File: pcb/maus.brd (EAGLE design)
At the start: 100 x 101 mm, 79 parts, among them IC1 AP1509-50SG-13, J1 SS-52300-001, Q2 BSS123, Q3 BSS123, Q4 BSS123, Q6 PMN30XPEA, Q7 PMN30XPEA, U2 CH340C, U4 LP3965EMP-3.3, U6 LM358DR, U69 ESP32-S2-WROOM

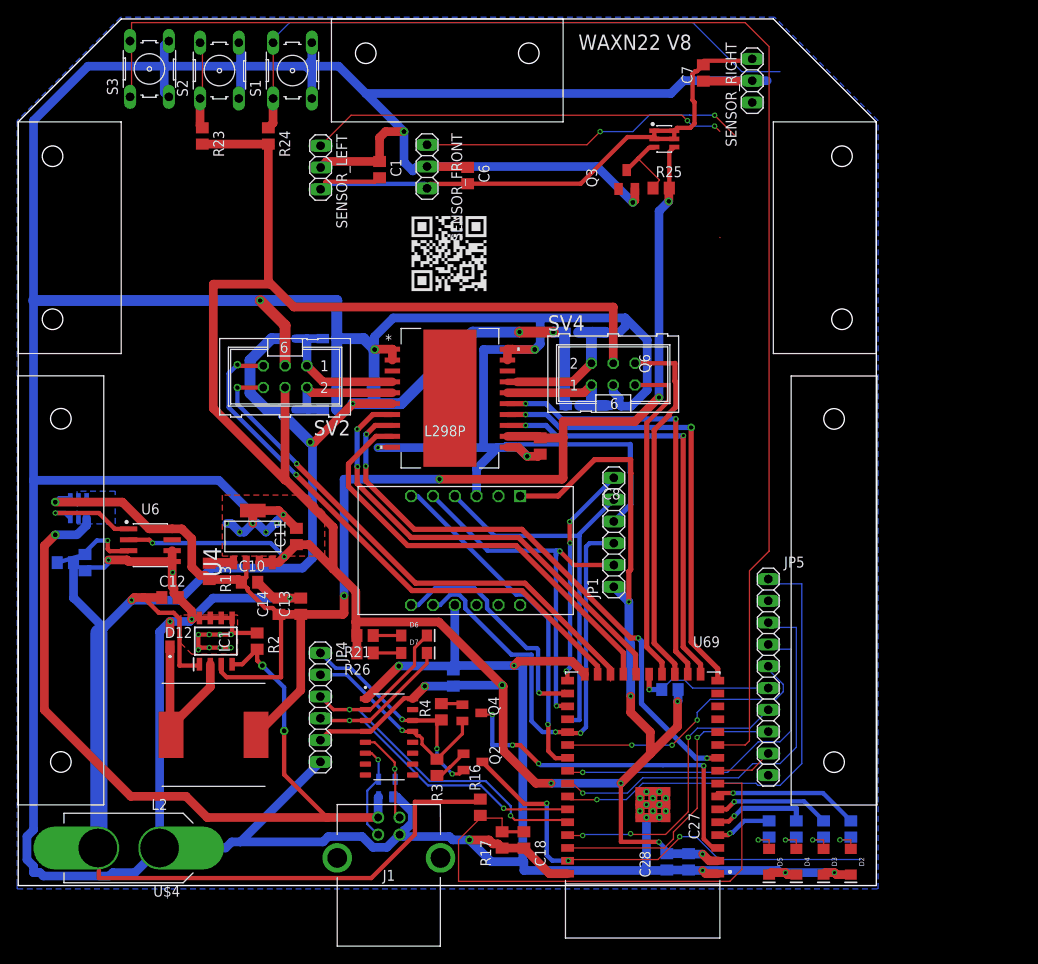
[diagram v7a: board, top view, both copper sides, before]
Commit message: update sensor + btn wiring
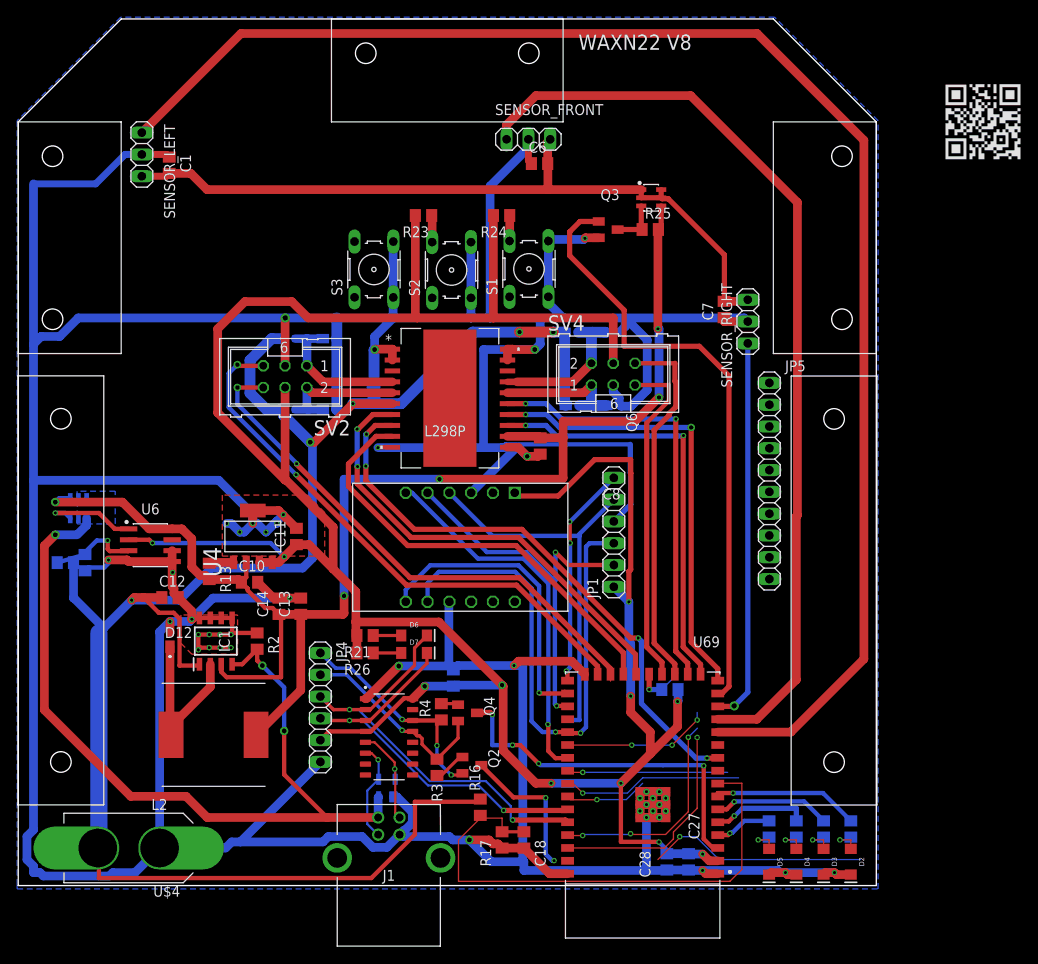
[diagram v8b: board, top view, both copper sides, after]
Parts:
- moved S1 36.0 mm to (75.5, 86.9)
- moved S2 35.7 mm to (66.5, 86.7)
- moved S3 35.1 mm to (57.5, 86.8)
- moved R24 28.7 mm to (72.3, 93.1), turned to 180 degrees
- moved SENSOR_RIGHT 28.1 mm to (101.0, 80.7)
- moved C7 27.7 mm to (98.3, 82.1)
- moved R23 27.4 mm to (63.2, 93.1), turned to 180 degrees
- moved C1 24.5 mm to (33.6, 98.9)
- moved JP5 22.9 mm to (103.5, 62.1)
- moved SENSOR_LEFT 20.9 mm to (30.4, 100.2)
- moved SENSOR_FRONT 12.2 mm to (75.5, 102.0), turned to 0 degrees
- moved C6 8.50 mm to (76.8, 99.1), turned to 0 degrees
- moved Q6 7.03 mm to (89.8, 95.2)
- moved Q3 6.23 mm to (84.8, 91.4), turned to 270 degrees
- moved R25 4.99 mm to (89.7, 91.5)
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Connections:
- net SENSOR_FRONT: now also U69.13; no longer U69.14
- net SENSOR_LEFT: now also U69.12; no longer U69.13
- net SENSOR_RIGHT: now also U69.14; no longer U69.12
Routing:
- net N$1: track 170.1 -> 0.14 mm
- net SENSOR_LEFT: track 48.8 -> 175.1 mm, vias 2 -> 0
- net GND: track 821.0 -> 731.1 mm, vias 32 -> 31
- net ESP32_EN: track 128.1 -> 45.9 mm
- net SENSOR_EN: track 0.00 -> 71.3 mm
- net SENSOR_FRONT: track 38.3 -> 108.9 mm, vias 2 -> 0
- net DRDY_A/G: track 54.7 -> 9.70 mm
- net SENSOR_RIGHT: track 0.00 -> 44.9 mm, vias 0 -> 1
- net INT_A/G: track 47.1 -> 21.1 mm
- net INT_M: track 40.7 -> 18.7 mm
- net N$7: track 73.0 -> 87.7 mm
- net DRDY_M: track 32.4 -> 17.7 mm
- net IO18: track 16.5 -> 4.79 mm
- net IO45: track 35.4 -> 25.5 mm
- net IO46: track 34.3 -> 25.7 mm
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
